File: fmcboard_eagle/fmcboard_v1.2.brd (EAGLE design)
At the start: 136 x 74 mm, 88 parts, among them IC1 OPA699ID, IC10 LTC6229IMS8E#TRPBF, IC11 LTC6229IMS8E#TRPBF, IC2 LM2662M_NOPB, IC3 LTC6229IMS8E#TRPBF, IC4 LTC6229IMS8E#TRPBF, IC5 LM358, IC6 OPA699ID, IC7 OPA699ID, IC8 LTC6229IMS8E#TRPBF, IC9 LTC6229IMS8E#TRPBF, J1 8pin, J12 4p-2.54, J2 ASP-134604-01, J3 4p-2.54, J4 4p-2.54, J5 8pin, U1 TXS0108EPWR

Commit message: Before routing
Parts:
- added J6, J7: 4p-2.54, Seeed-Connector:H4-2.54
- added R49: 50, SparkFun-Resistors:AXIAL-0.3
- moved U1 50.2 mm to (68.0, 68.0), flipped to the top
- moved C9 43.0 mm to (66.0, 61.0), flipped to the top
- moved C14 39.2 mm to (70.0, 61.0), flipped to the top, turned to 180 degrees
- moved R10 37.9 mm to (54.0, 32.0)
- moved R9 37.9 mm to (54.0, 35.0)
- moved R17 34.0 mm to (54.0, 24.0)
- moved R3 34.0 mm to (54.0, 27.0)
- moved R25 28.4 mm to (79.0, 30.0)
- moved R37 25.0 mm to (43.0, 59.0)
- moved R6 25.0 mm to (54.0, 49.0)
- moved R19 20.1 mm to (54.0, 39.0)
- moved R18 20.0 mm to (54.0, 42.0)
- moved R26 20.0 mm to (54.0, 46.0)
- moved SV2 20.0 mm to (28.0, 27.0)
- moved R45 20.0 mm to (43.0, 39.0)
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- renumbered R1 to R_O1, R12 to R_O2, R7 to R_VH, R8 to R_VL
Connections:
- new net TRANSIN: IC4.2, R11.2, R49.P$1
- net GND: now also J1.1, J1.2, J1.7, J1.8
- net IO1: now also R49.P$2; no longer IC4.2, R11.2
- net VS+: now also J6.1, J6.2, J6.3, J6.4
- net VS-: now also J7.1, J7.2, J7.3, J7.4
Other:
- board size 136 x 74 mm -> 125 x 74 mm
- board text added: "N1"
- board text added: "N2"
- board text added: "N3"
- board text added: "N4"
- board text added: "OFFSETIN2"
- board text added: "OP2BUF"
- board text added: "OPOUT1 H10"
- board text added: "OPOUT2 H11"
- board text added: "Offset1"
- board text added: "Offset2"
- board text added: "P1"
- board text added: "P2"
- board text added: "P3"
- board text added: "P4"
- board text added: "PULSESUMOUT"
- board text added: "Series"
- board text added: "TRANSOUT"
- board text added: "VS+"
- board text added: "VS-"
- board text removed: "AR SCLIN"
- board text removed: "AR SDAIN"
- board text removed: "IO H11"
- board text removed: "OPBUF1"
- board text removed: "OPBUF2"
- board text removed: "OPOUT H10"
- board text removed: "Off Adj"
- board text removed: "VH Adj"
- board text removed: "VL Adj"

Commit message: v1.2
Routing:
- net VS+: track 0.00 -> 358.4 mm, vias 0 -> 7
- net VS-: track 0.00 -> 283.5 mm, vias 0 -> 11
- net OPOUT1_H10: track 0.00 -> 215.3 mm, vias 0 -> 4
- net OPOUT2_H11: track 0.00 -> 212.0 mm, vias 0 -> 8
- net H37: track 0.00 -> 157.4 mm, vias 0 -> 4
- net VH: track 0.00 -> 149.7 mm, vias 0 -> 6
- net C15: track 0.00 -> 147.3 mm, vias 0 -> 3
- net SDAIN: track 0.00 -> 142.6 mm, vias 0 -> 4
- net H38: track 0.00 -> 141.2 mm, vias 0 -> 4
- net SCLIN: track 0.00 -> 137.4 mm, vias 0 -> 2
- net GND: track 0.00 -> 136.6 mm, vias 0 -> 10
- net OFFSETIN1: track 0.00 -> 136.4 mm, vias 0 -> 4
- net H35: track 0.00 -> 135.9 mm, vias 0 -> 5
- net H34: track 0.00 -> 135.0 mm, vias 0 -> 5
- net VL: track 0.00 -> 132.3 mm, vias 0 -> 6
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
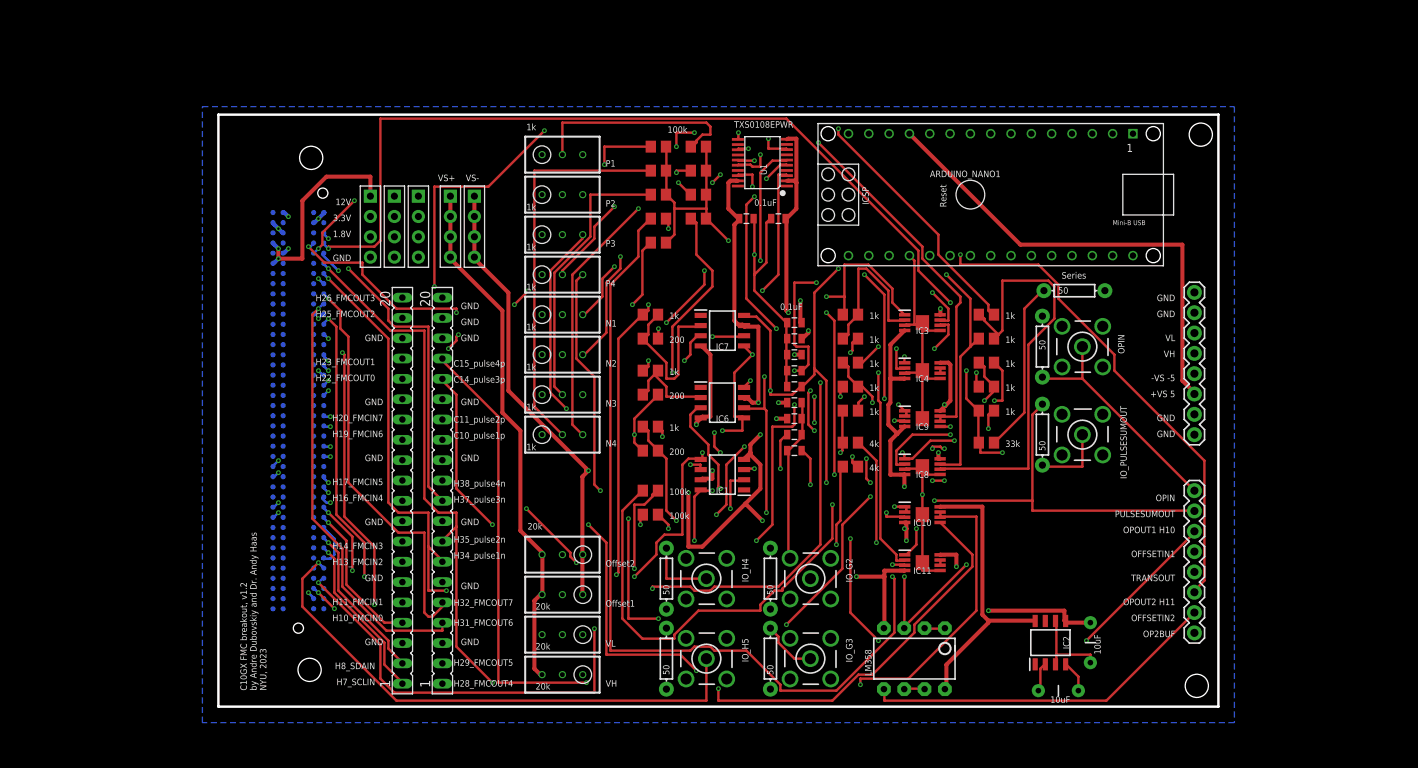
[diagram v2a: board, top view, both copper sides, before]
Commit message: v1.21 make exposed pads VS- not GND, divide voltage before op amp buffers, add op amp decoupling caps, improve layout
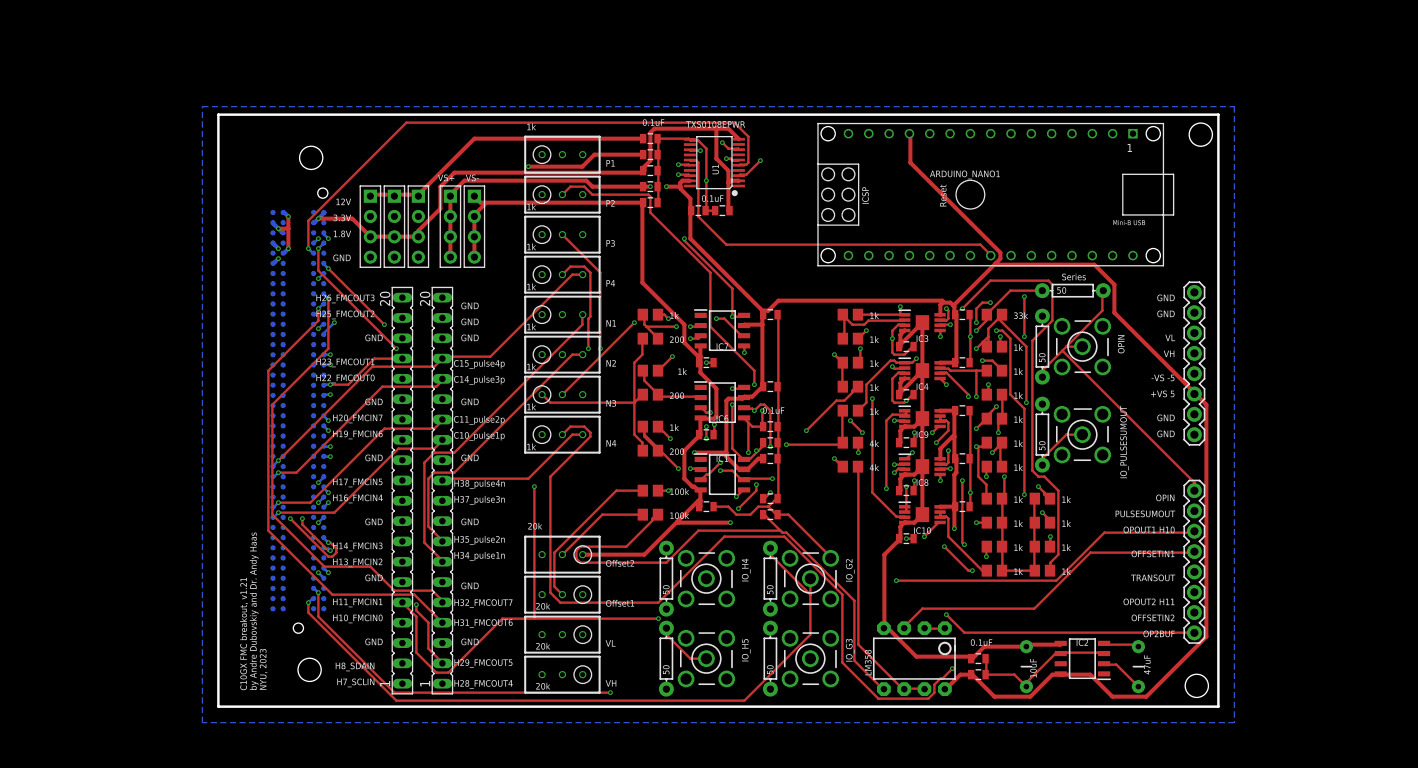
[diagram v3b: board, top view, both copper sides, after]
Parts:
- removed IC11: LTC6229IMS8E#TRPBF, LTC6229IMS8E#TRPBF:SOP65P490X110-9N
- removed R42, R44, R46, R48: 100k, rcl:R0805
- added C15, C16, C17, C18, C19, C20, C21, C22, C23, C24, C25, C26, C27, C28, C29, C30, C31, C6: 0.1uF, SparkFun-Passives:0805
- added R1, R12, R7, R8: 1k, rcl:R0805
- C1: value 10uF -> 47uF
- R32, R33, R36, R38, R40: value 100k -> 1k
- moved R36 67.6 mm to (97.0, 17.0)
- moved R32 65.9 mm to (103.0, 20.0), turned to 0 degrees
- moved R38 65.9 mm to (103.0, 17.0), turned to 0 degrees
- moved R33 56.6 mm to (97.0, 23.0), turned to 180 degrees
- moved R40 53.0 mm to (97.0, 26.0)
- moved C10 32.4 mm to (54.0, 63.0)
- moved C3 32.4 mm to (54.0, 65.0)
- moved C12 29.2 mm to (54.0, 71.0), turned to 0 degrees
- moved C13 29.2 mm to (54.0, 69.0), turned to 0 degrees
- moved C5 29.2 mm to (54.0, 67.0), turned to 0 degrees
- moved R30 19.0 mm to (97.0, 30.0), turned to 0 degrees
- moved R11 16.0 mm to (97.0, 49.0), turned to 180 degrees
- moved R29 13.0 mm to (97.0, 33.0)
- moved C1 10.4 mm to (115.0, 5.00), turned to 90 degrees
- moved C11 8.54 mm to (69.0, 26.0)
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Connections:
- removed net N$15: R31.2, R32.2
- removed net N$16: IC11.6, IC11.7
- removed net N$17: IC11.3, R33.1
- removed net N$19: R35.2, R36.2
- removed net N$20: R37.2, R38.2
- removed net N$21: R39.2, R40.2
- removed net N$22: R41.2, R42.2
- removed net N$23: R43.2, R44.2
- removed net N$24: R45.2, R46.2
- removed net N$25: R47.2, R48.2
- removed net N$7: IC4.6, IC4.7
- new net N$27: IC4.5, R1.1
- new net PULSEINN1: R22.2, R41.2
- new net PULSEINN2: R24.1, R43.2
- new net PULSEINN3: R28.2, R45.2
- new net PULSEINN4: R30.1, R47.2
- new net PULSEINP1: IC9.3, R31.2
- new net PULSEINP2: IC9.5, R35.2
- new net PULSEINP3: IC10.3, R37.2
- new net PULSEINP4: IC10.5, R39.2
- net C10: now also R31.3; no longer IC9.3
- net C11: now also R35.3; no longer IC9.5
- net C14: now also R37.3; no longer IC10.3
- net C15: now also R39.3; no longer IC10.5
- net GND: now also C15.2, C16.2, C17.2, C18.2, C19.2, C20.2, C21.2, C22.2, C23.2, C24.2, C25.2, C26.2, C27.2, C28.2, C29.2, C30.2, C31.2, C6.2; no longer IC10.9, IC11.5, IC11.9, IC3.9, IC4.5, IC4.9, IC8.9, IC9.9
- net H34: now also R41.3; no longer R22.2
- net H35: now also R43.3; no longer R24.1
- net H37: now also R45.3; no longer R28.2
- net H38: now also R47.3; no longer R30.1
- net PULSEOUTN1: now also R12.2; no longer R41.3
- net PULSEOUTN2: now also R38.2; no longer R43.3
- net PULSEOUTN3: now also R32.2; no longer R45.3
- net PULSEOUTN4: now also R40.2; no longer R47.3
- net PULSEOUTP1: now also R7.2; no longer R31.3
- net PULSEOUTP2: now also R33.2; no longer R35.3
- net PULSEOUTP3: now also R8.2; no longer R37.3
- net PULSEOUTP4: now also R36.2; no longer R39.3
- net PULSESUMIN: now also IC4.6, R12.1, R33.1, R7.1, R8.1; no longer IC11.2, R42.1, R44.1, R46.1, R48.1
- net PULSESUMOUT: now also IC4.7, R1.2; no longer IC11.1, R33.2
- net VS+: now also C16.1, C18.1, C20.1, C22.1, C24.1, C26.1, C28.1, C30.1, C6.1; no longer IC11.8
- net VS-: now also C15.1, C17.1, C19.1, C21.1, C23.1, C25.1, C27.1, C29.1, C31.1, IC10.9, IC3.9, IC4.9, IC8.9, IC9.9; no longer IC11.4
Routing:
- net PULSEINN4: track 0.00 -> 124.7 mm, vias 0 -> 4
- net N$17: track 107.7 -> 0.00 mm, vias 2 -> 0
- net PULSEOUTP4: track 114.1 -> 10.6 mm, vias 4 -> 0
- net C15: track 147.3 -> 48.8 mm, vias 3 -> 1
- net PULSEINP1: track 0.00 -> 94.3 mm, vias 0 -> 3
- net H37: track 157.4 -> 66.3 mm, vias 4 -> 2
- net PULSEOUTN4: track 104.9 -> 14.9 mm
- net H38: track 141.2 -> 59.0 mm, vias 4 -> 1
- net PULSEINP3: track 0.00 -> 79.6 mm, vias 0 -> 2
- net C14: track 129.4 -> 52.1 mm, vias 7 -> 1
- net OPOUT1_H10: track 215.3 -> 138.7 mm, vias 4 -> 5
- net PULSEINN3: track 0.00 -> 73.7 mm, vias 0 -> 2
- net PULSESUMOUT: track 114.8 -> 44.7 mm, vias 5 -> 1
- net PULSEINP4: track 0.00 -> 69.3 mm, vias 0 -> 4
- net PULSEINP2: track 0.00 -> 67.4 mm, vias 0 -> 4
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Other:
- board text added: "C10GX FMC breakout, v1.21 by Andre Dubovskiy and Dr. Andy Haas NYU, 2023"
- board text removed: "C10GX FMC breakout, v1.2 by Andre Dubovskiy and Dr. Andy Haas NYU, 2023"

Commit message: Fixes for v1.21, amps etc
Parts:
- removed R49: 50, SparkFun-Resistors:AXIAL-0.3
- added C32, C34, C35, C36, C37: 5pF, SparkFun-Passives:0805
- added C33: 2pF, SparkFun-Passives:0805
- R11: value 33k -> 5k
- R2: device SparkFun-Resistors:AXIAL-0.3 -> rcl:R0805
- moved R2 7.21 mm to (107.0, 51.0), turned to 0 degrees
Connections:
- removed net N$27: IC4.5, R1.1
- net GND: now also IC4.5; no longer R2.P$1
- net IO1: now also R2.2; no longer R2.P$2, R49.P$2
- net N$12: now also C35.2
- net N$13: now also C34.2
- net N$14: now also C37.1
- net N$4: now also C36.1
- net PULSEINN1: now also C34.1
- net PULSEINN2: now also C36.2
- net PULSEINN3: now also C35.1
- net PULSEINN4: now also C37.2
- net PULSESUMIN: now also C32.1, R1.1
- net PULSESUMOUT: now also C32.2
- net TRANSIN: now also C33.1, R2.1; no longer R49.P$1
- net TRANSOUT: now also C33.2
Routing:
- net N$27: track 9.92 -> 0.00 mm, vias 2 -> 0
- net PULSESUMIN: track 42.2 -> 48.5 mm, vias 2 -> 4
- net GND: track 159.3 -> 165.0 mm

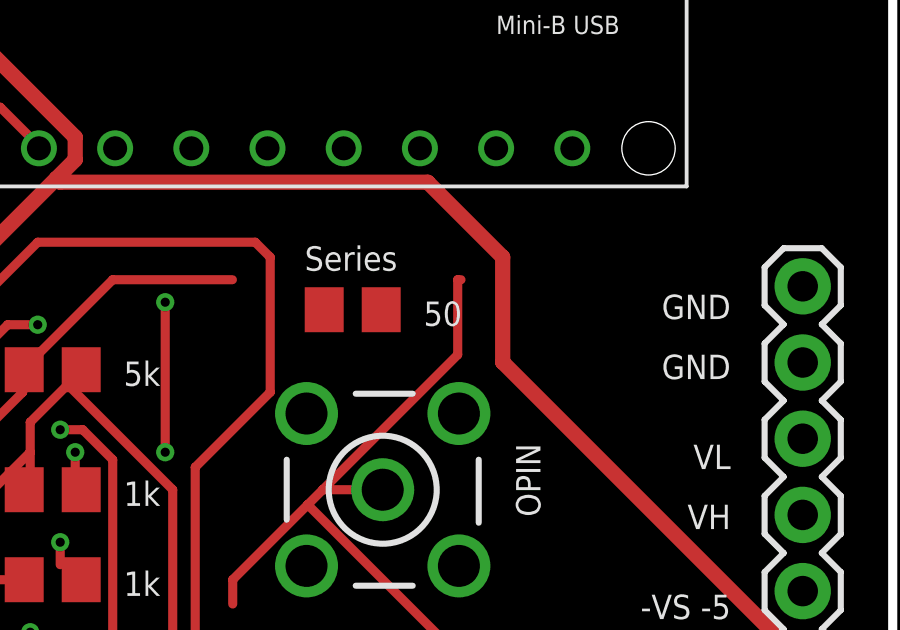
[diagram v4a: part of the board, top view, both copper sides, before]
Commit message: Tune the trans amp gain and compensation
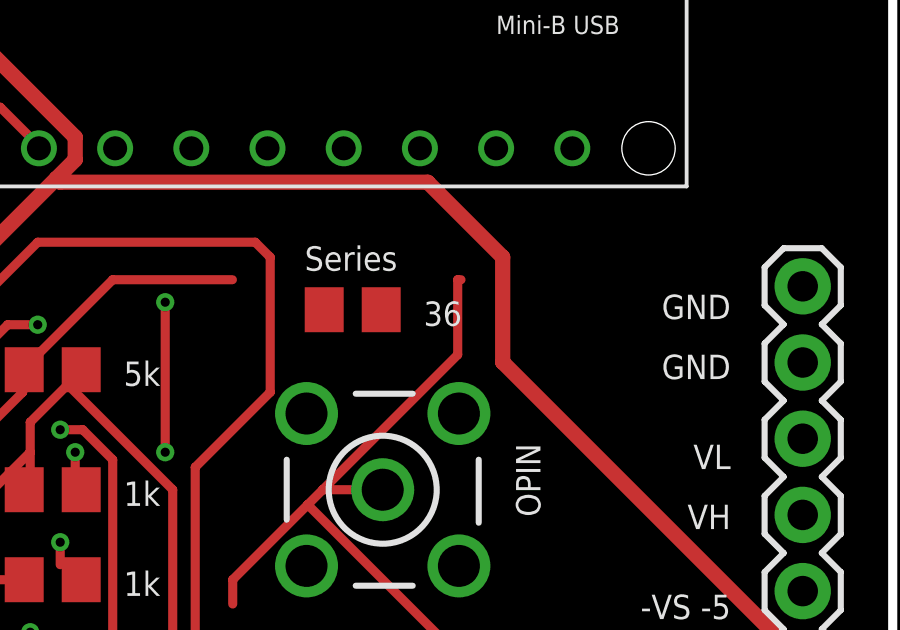
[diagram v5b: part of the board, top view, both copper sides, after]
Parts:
- C33: value 2pF -> 1pF
- R2: value 50 -> 36
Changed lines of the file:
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@@
 <drawing>
 <settings>
-<setting alwaysvectorfont="yes"/>
+<setting alwaysvectorfont="no"/>
 <setting verticaltext="up"/>
 </settings>
@@
 <attribute name="VALUE" x="99.365" y="25.46" size="0.8128" layer="21"/>
 </element>
-<element name="R2" library="rcl" library_urn="urn:adsk.eagle:library:334" package="R0805" package3d_urn="urn:adsk.eagle:package:23553/2" value="50" x="107" y="51" smashed="yes">
+<element name="R2" library="rcl" library_urn="urn:adsk.eagle:library:334" package="R0805" package3d_urn="urn:adsk.eagle:package:23553/2" value="36" x="107" y="51" smashed="yes">
 <attribute name="POPULARITY" value="85" x="107" y="51" size="1.778" layer="27" display="off"/>
 <attribute name="SPICEPREFIX" value="R" x="107" y="51" size="1.778" layer="27" display="off"/>
@@
 <attribute name="VALUE" x="-22.016" y="-6.397" size="0.4064" layer="27"/>
 </element>
-<element name="C33" library="SparkFun-Passives" package="0805" value="2pF" x="-24" y="-5" smashed="yes">
+<element name="C33" library="SparkFun-Passives" package="0805" value="1pF" x="-24" y="-5" smashed="yes">
 <attribute name="NAME" x="-24.762" y="-4.1745" size="0.4064" layer="25"/>
 <attribute name="VALUE" x="-25.016" y="-6.397" size="0.4064" layer="27"/>
